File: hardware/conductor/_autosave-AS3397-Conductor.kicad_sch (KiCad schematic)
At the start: 49 parts, among them J1 Micro_SD_Card, J10 Conn_FX_2, J11 I2C controller, J12 Conn_01x03_Socket_AudioOUT, J13 Voice connector, J14 Conn_01x02_Socket, J15 I2C controller, J16 Conn_01x06_Socket_SPI, J17 Conn_01x03_Socket, J18 Conn_01x03_Socket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

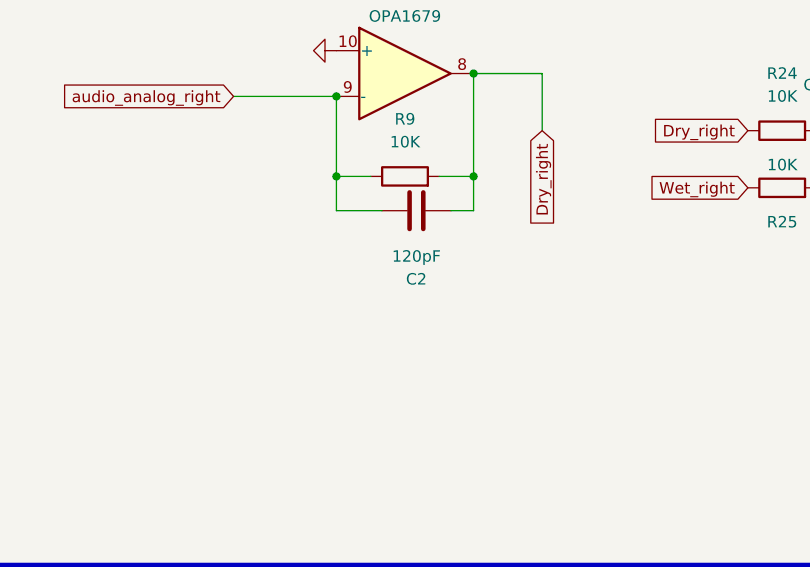
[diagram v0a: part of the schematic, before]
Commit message: Conductor Board : Fixing MIDI routing
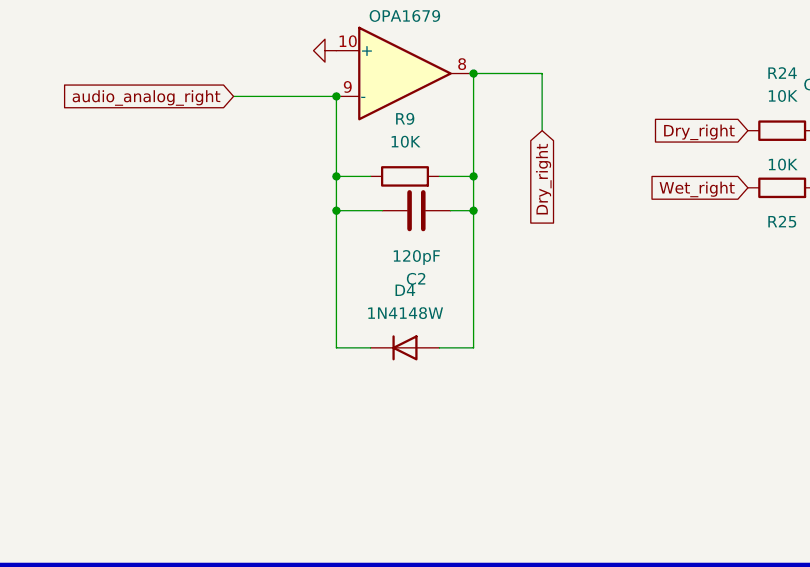
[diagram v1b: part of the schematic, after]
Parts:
- added D4: 1N4148W, Diode_SMD:D_SOD-123, symbol Diode:1N4148W
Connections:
- net Dry_right: now also D4.2 (A)
- net audio_analog_right: now also D4.1 (K)
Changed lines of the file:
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@@
 	)
 	(junction
+		(at 219.71 80.01)
+		(diameter 0)
+		(color 0 0 0 0)
+	)
+	(junction
 		(at 279.4 68.58)
 		(diameter 0)
@@
 	)
 	(junction
+		(at 204.47 80.01)
+		(diameter 0)
+		(color 0 0 0 0)
+	)
+	(junction
 		(at 204.47 76.2)
 		(diameter 0)
@@
 	(wire
 		(pts
+			(xy 219.71 95.25) (xy 215.9 95.25)
+		)
+		(stroke
+			(width 0)
+			(type default)
+		)
+	)
+	(wire
+		(pts
+			(xy 219.71 80.01) (xy 219.71 95.25)
+		)
+		(stroke
+			(width 0)
+			(type default)
+		)
+	)
+	(wire
+		(pts
 			(xy 219.71 64.77) (xy 227.33 64.77)
 		)
@@
 	(wire
 		(pts
+			(xy 204.47 95.25) (xy 208.28 95.25)
+		)
+		(stroke
+			(width 0)
+			(type default)
+		)
+	)
+	(wire
+		(pts
 			(xy 278.13 41.91) (xy 278.13 31.75)
 		)
@@
 	(wire
 		(pts
+			(xy 204.47 80.01) (xy 204.47 95.25)
+		)
+		(stroke
+			(width 0)
+			(type default)
+		)
+	)
+	(wire
+		(pts
 			(xy 83.82 133.35) (xy 82.55 133.35)
 		)
@@
 					(unit 1)
 				)
+			)
+		)
+	)
+	(symbol
+		(lib_id "Diode:1N4148W")
+		(at 212.09 95.25 0)
+		(unit 1)
+		(exclude_from_sim no)
+		(in_bom yes)
+		(on_board yes)
+		(dnp no)
+		(fields_autoplaced yes)
+		(property "Reference" "D4"
+			(at 212.09 88.9 0)
+			(effects
+				(font
+					(size 1.27 1.27)
+				)
+			)
+		)
+		(property "Value" "1N4148W"
+			(at 212.09 91.44 0)
+			(effects
+				(font
+					(size 1.27 1.27)
+				)
+			)
+		)
+		(property "Footprint" "Diode_SMD:D_SOD-123"
+			(at 212.09 99.695 0)
+			(effects
+				(font
+					(size 1.27 1.27)
+				)
+				(hide yes)
+			)
+		)
+		(property "Datasheet" "https://www.vishay.com/docs/85748/1n4148w.pdf"
+			(at 212.09 95.25 0)
+			(effects
+				(font
+					(size 1.27 1.27)
+				)
+				(hide yes)
+			)
+		)
+		(property "Description" "75V 0.15A Fast Switching Diode, SOD-123"
+			(at 212.09 95.25 0)
+			(effects
+				(font
+					(size 1.27 1.27)
+				)
+				(hide yes)
+			)
+		)
+		(property "Sim.Device" "D"
+			(at 212.09 95.25 0)
+			(effects
+				(font
+					(size 1.27 1.27)
+				)
+				(hide yes)
+			)
+		)
+		(property "Sim.Pins" "1=K 2=A"
+			(at 212.09 95.25 0)
+			(effects
+				(font
+					(size 1.27 1.27)
+				)
+				(hide yes)
+			)
+		)
+		(pin "2"
+		)
+		(pin "1"
+		)
+		(instances
+			(project ""
+				(path "/1142383e-caad-4ba6-b094-d0948c22312a"
+					(reference "D4")
+					(unit 1)
+				)
